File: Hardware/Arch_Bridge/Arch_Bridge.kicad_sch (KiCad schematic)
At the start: 91 parts, among them J1 Conn_01x02, J3 Conn_01x04, J4 Conn_01x04, Q1 2N3904, Q2 MJE2955, Q3 MJE2955, U1 AP63205WU, U11 ESP32-S3-WROOM-1, U12 TXS0102DCT, U13 DRV8231ADDAR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

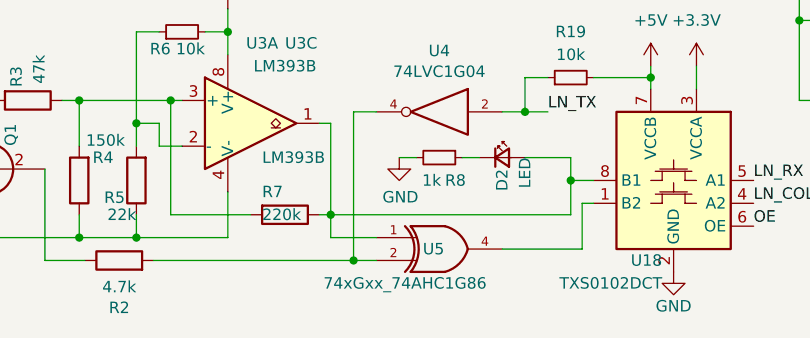
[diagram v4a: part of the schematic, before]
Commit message: More predictable Loconet TX_Q speeds. RX_Q similarly optimized, but continues to show high mS spike. Crashes on collision detect.
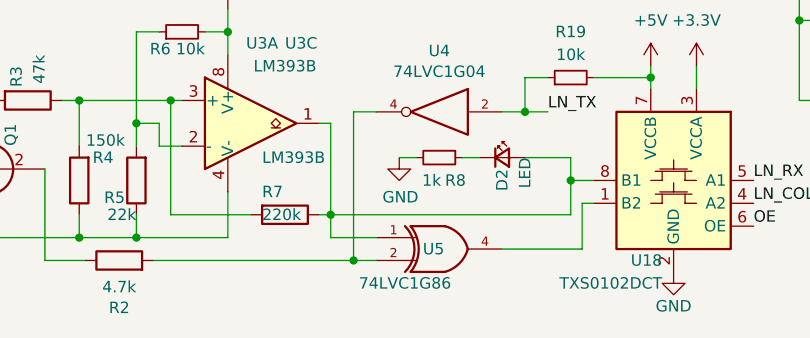
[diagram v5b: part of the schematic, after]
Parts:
- BOOT1, RESET1: LCSC SKU (none) -> C231329
- C1, C2, C3, C4: LCSC SKU (none) -> C2164091
- C10, C11, C5, C7, C8, C9, CU11, CU6: LCSC SKU (none) -> C600013
- C6: LCSC SKU (none) -> C2223641
- CB1: LCSC SKU (none) -> C2831718
- D3, D5: LCSC SKU (none) -> C895239
- D6: LCSC SKU (none) -> C523217
- D9: LCSC SKU (none) -> C552812
- F2, F3: LCSC SKU (none) -> C2442492
- F4: LCSC SKU (none) -> C2153889
- JP1: LCSC SKU (none) -> C5172712
- JP2, JP3: LCSC SKU (none) -> C3326988
- L1: LCSC SKU (none) -> C167828
- LOCONET_B1, LOCONET_B2, LOCONET_T1: LCSC SKU (none) -> C4355015
- Q1: LCSC SKU (none) -> C2980867
- Q2, Q3: LCSC SKU (none) -> C184196
- R1, R21, R24, R8: LCSC SKU (none) -> C131398
- R10: LCSC SKU (none) -> C488764
- R11, R12: LCSC SKU (none) -> C132648
- R13: LCSC SKU (none) -> C706423
- R14: LCSC SKU (none) -> C1391077
- R15: LCSC SKU (none) -> C872782
- R16, R17, R19, R20, R6: LCSC SKU (none) -> C4303232
- R18: LCSC SKU (none) -> C870936
- R2: LCSC SKU (none) -> C3975500
- R22, R23, R3: LCSC SKU (none) -> C137270
- R4: LCSC SKU (none) -> C114931
- R5: LCSC SKU (none) -> C114942
- R7: LCSC SKU (none) -> C130275
- R9: LCSC SKU (none) -> C601882; MFG YAEGO -> C601882
- U1: LCSC SKU (none) -> C2071056
- U11: LCSC SKU (none) -> C2980298
- U12, U17, U18: LCSC SKU (none) -> C2677354
- U19, U20: LCSC SKU (none) -> C17206
- U2: LCSC SKU (none) -> C91728
- U3: LCSC SKU (none) -> C2865059
- U4, U? (x2): LCSC SKU (none) -> C7827
- U5: value 74xGxx_74AHC1G86 -> 74LVC1G86; LCSC SKU (none) -> C402161; PN SN74LVC1G02DBVR -> SN74LVC1G86DBVR
- U6: LCSC SKU (none) -> C150160
- U? (x4): LCSC SKU (none) -> C2682152
- USB1: LCSC SKU (none) -> C136000

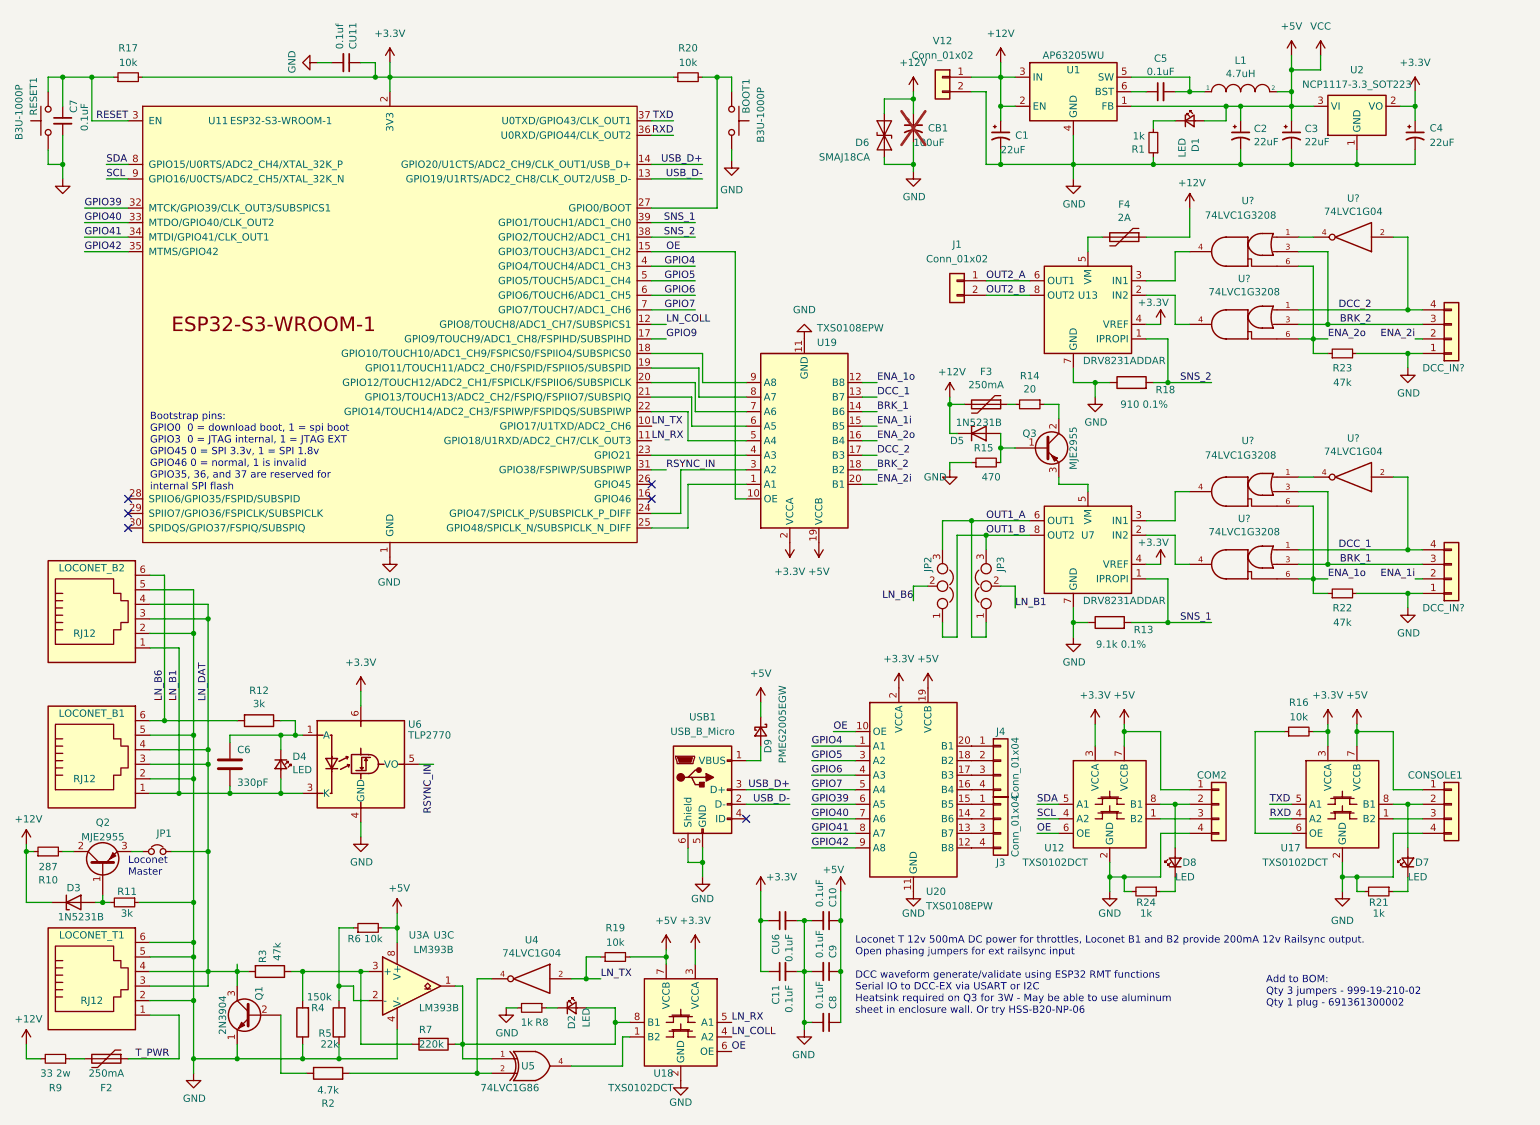
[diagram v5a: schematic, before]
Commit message: Schematic rev 0.8, PCB update adding current sense filter caps, fixing pull-up on Loconet TX, and slight reposition of U17
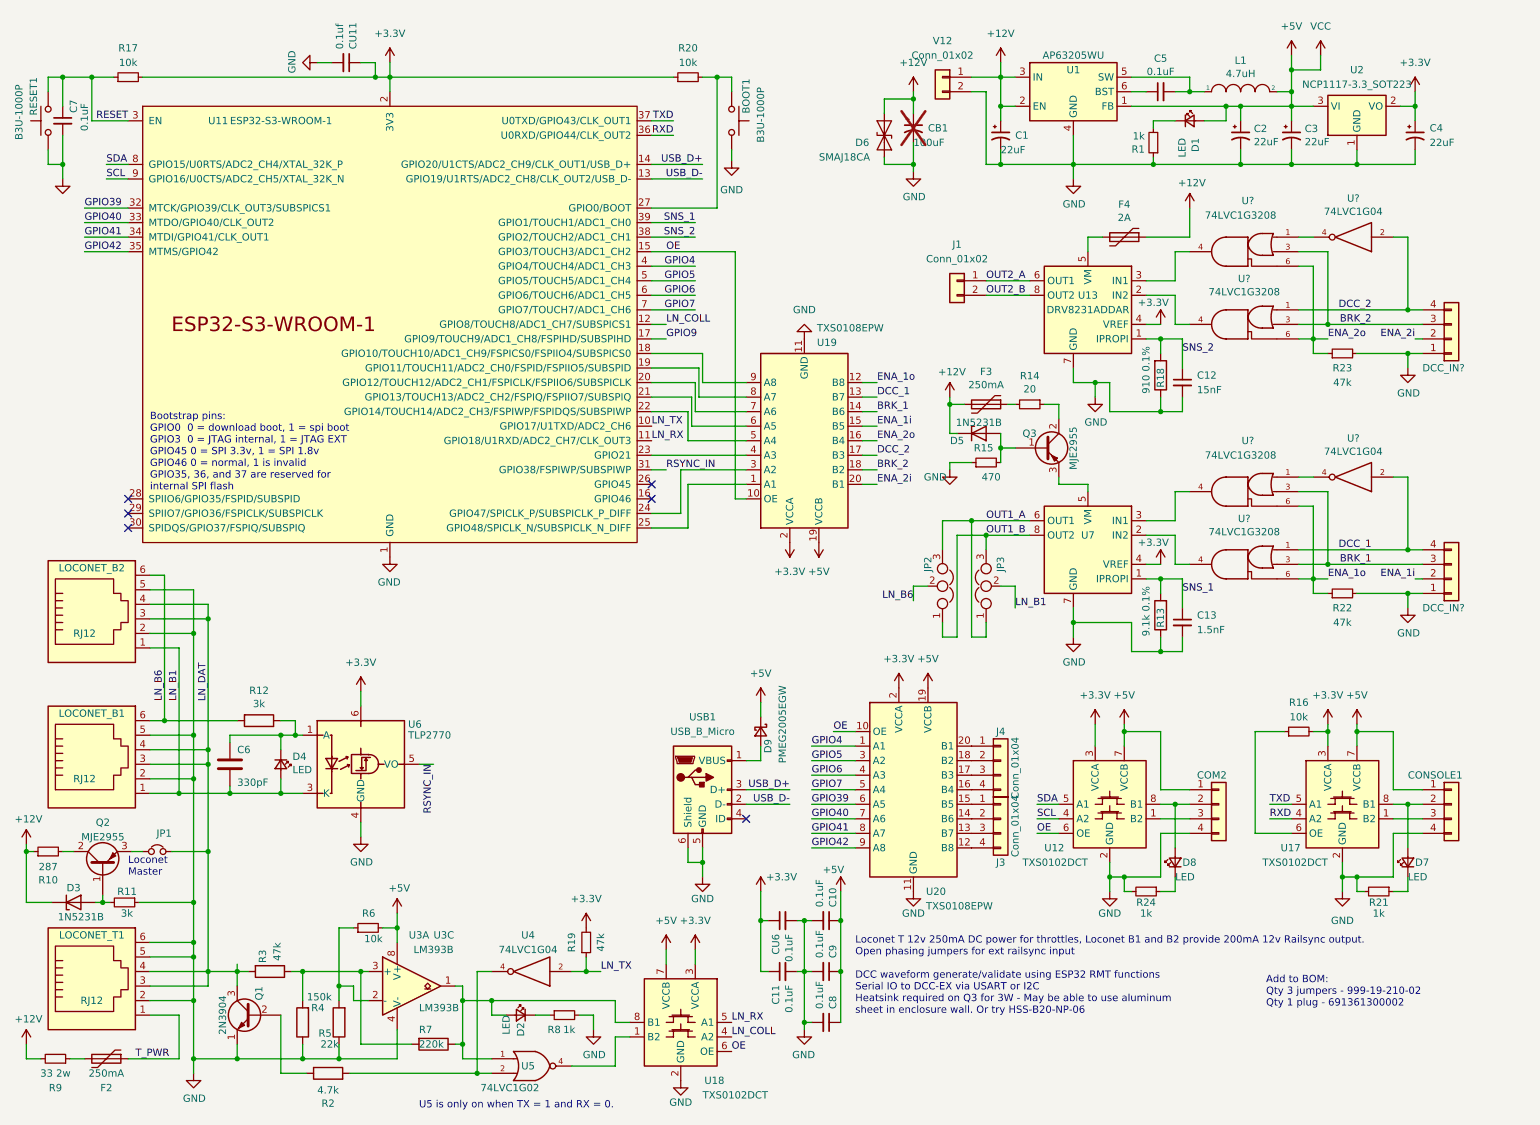
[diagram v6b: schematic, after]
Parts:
- added C12: 15nF, Capacitor_SMD:C_1206_3216Metric_Pad1.33x1.80mm_HandSolder, symbol Device:C_Small
- added C13: 1.5nF, Capacitor_SMD:C_1206_3216Metric_Pad1.33x1.80mm_HandSolder, symbol Device:C_Small
- R19: value 10k -> 47k; PN RC1206FR-1310KL -> RC1206FR-0747KL
- U5: value 74LVC1G86 -> 74LVC1G02; symbol Loconet DCC Interface-rescue:74AHC1G86-74xGxx -> Loconet DCC Interface-rescue:74AHCT1G02-74xGxx
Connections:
- net +3.3V: now also R19.2
- net +5V: no longer R19.2
- net GND: now also C12.2, C13.2
- net SNS_1: now also C13.1
- net SNS_2: now also C12.1
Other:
- note added: "Loconet T 12v 250mA DC power for throttles, Loconet B1 and B2 provide 200mA 12v Railsync output. Open phasing jumpers for ext railsync input DCC waveform generate/validate using ESP32 RMT functions Serial IO to DCC-EX via USART or I2C Heatsink required on Q3 for 3W - May be able to use aluminum sheet in enclosure wall. Or try HSS-B20-NP-06"
- note added: "U5 is only on when TX = 1 and RX = 0."
- note removed: "Loconet T 12v 500mA DC power for throttles, Loconet B1 and B2 provide 200mA 12v Railsync output. Open phasing jumpers for ext railsync input DCC waveform generate/validate using ESP32 RMT functions Serial IO to DCC-EX via USART or I2C Heatsink required on Q3 for 3W - May be able to use aluminum sheet in enclosure wall. Or try HSS-B20-NP-06"
- moved on the sheet: D2, R13, R18, R19, R8, U4

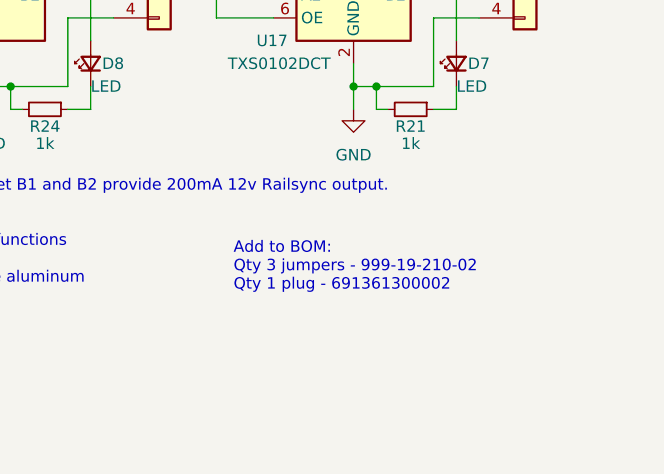
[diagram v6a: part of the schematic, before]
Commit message: Changed aux track output to use 5.0mm pitch matching EX-8874 track plugs
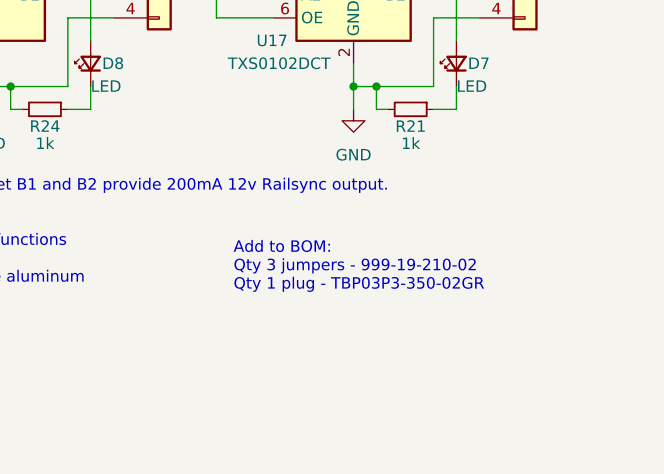
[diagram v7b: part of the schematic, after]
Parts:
- J1: footprint Terminal_Wuerth_new:WR-TBL 2P -> Connector_Phoenix_MC:PhoenixContact_MC_1,5_2-G-3.5_1x02_P3.50mm_Horizontal; LCSC SKU (none) -> C880572; MFG Wuerth Electronik -> CUI Inc; PN 691322310002 -> TBP03R1-350-02GR
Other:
- note added: "Add to BOM: Qty 3 jumpers - 999-19-210-02 Qty 1 plug - TBP03P3-350-02GR"
- note removed: "Add to BOM: Qty 3 jumpers - 999-19-210-02 Qty 1 plug - 691361300002"
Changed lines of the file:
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@@
     (effects (font (size 1.27 1.27)) (justify left bottom))
   )
-  (text "Add to BOM: \nQty 3 jumpers - 999-19-210-02\nQty 1 plug - 691361300002"
+  (text "Add to BOM: \nQty 3 jumpers - 999-19-210-02\nQty 1 plug - TBP03P3-350-02GR "
     (at 231.775 185.42 0)
     (effects (font (size 1.27 1.27)) (justify left bottom))
@@
       (effects (font (size 1.27 1.27)))
     )
-    (property "Footprint" "Terminal_Wuerth_new:WR-TBL 2P" (at 177.8 58.42 0)
+    (property "Footprint" "Connector_Phoenix_MC:PhoenixContact_MC_1,5_2-G-3.5_1x02_P3.50mm_Horizontal" (at 177.8 58.42 0)
       (effects (font (size 1.27 1.27)) hide)
     )
@@
       (effects (font (size 1.27 1.27)) hide)
     )
-    (property "MFG" "Wuerth Electronik" (at 177.8 58.42 0)
+    (property "MFG" "CUI Inc" (at 177.8 58.42 0)
       (effects (font (size 1.27 1.27)) hide)
     )
-    (property "PN" "691322310002 " (at 177.8 58.42 0)
+    (property "PN" "TBP03R1-350-02GR " (at 177.8 58.42 0)
       (effects (font (size 1.27 1.27)) hide)
     )
-    (property "LCSC SKU" "" (at 177.8 58.42 0)
+    (property "LCSC SKU" "C880572" (at 177.8 58.42 0)
       (effects (font (size 1.27 1.27)) hide)
     )

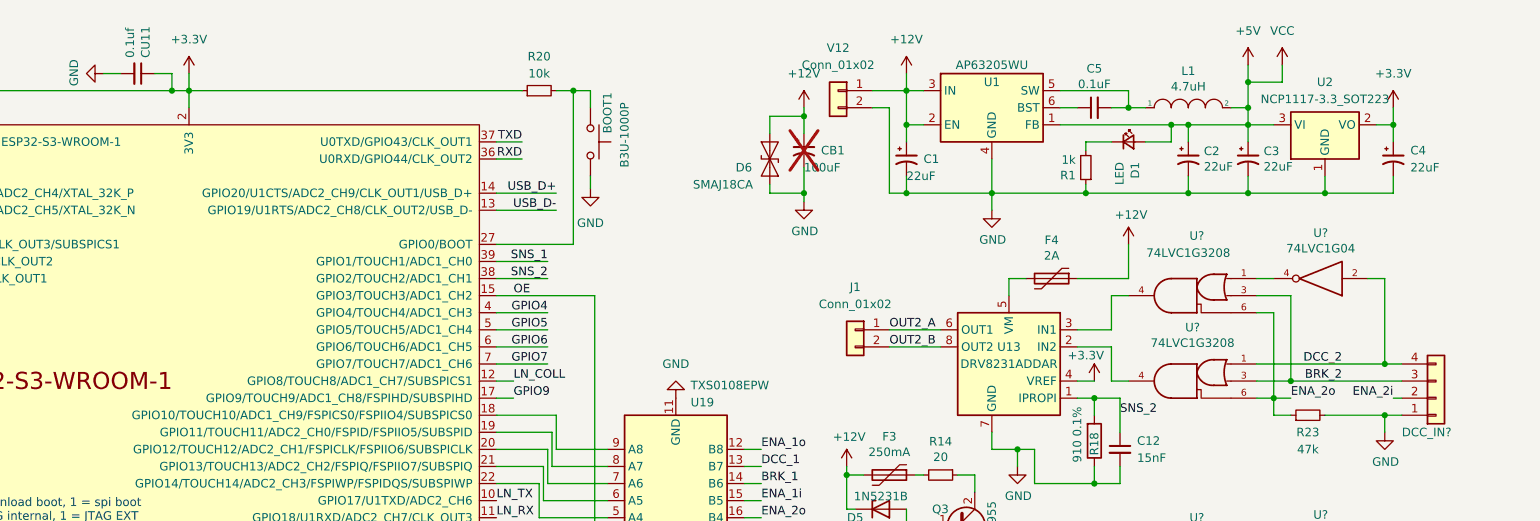
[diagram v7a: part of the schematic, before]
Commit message: Revised VIN to 5v power supply for better performance and less PCB space
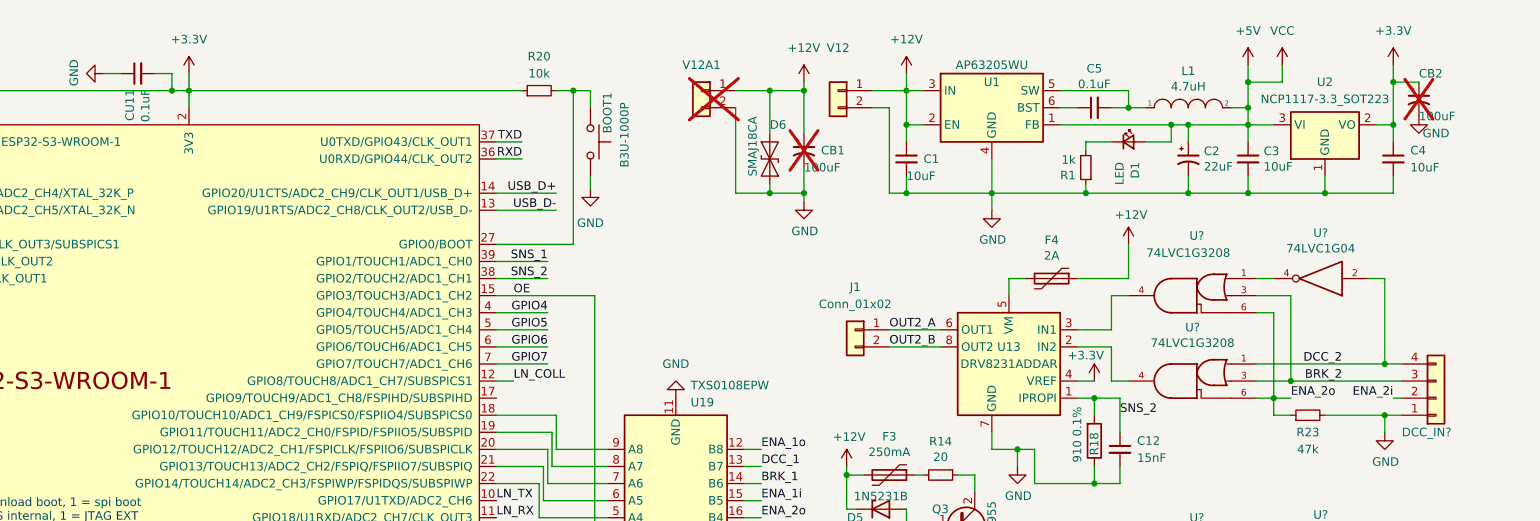
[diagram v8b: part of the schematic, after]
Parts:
- added CB2: 100uF, Capacitor_THT:CP_Radial_D6.3mm_P2.50mm, symbol Device:C_Polarized_Small_US
- added V12A1: Conn_01x02, Connector_Phoenix_MSTB:PhoenixContact_MSTBA_2,5_2-G_1x02_P5.00mm_Horizontal, symbol Connector_Generic:Conn_01x02
- C1, C3, C4: value 22uF -> 10uF; footprint Capacitor_SMD:CP_Elec_5x5.3 -> Capacitor_SMD:C_1210_3225Metric; symbol Device:C_Polarized_Small_US -> Device:C_Small; LCSC SKU C2164091 -> C2175202; MFG Wurth Electronik -> Murata; PN 865080542006 -> GRT31CR6YA106ME01L
- CU11: value 0.1uf -> 0.1uF
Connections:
- net +12V: now also V12A1.1 (Pin_1)
- net +3.3V: now also CU11.2, CB2.1; no longer CU11.1
- net GND: now also CU11.1, CB2.2, V12A1.2 (Pin_2); no longer CU11.2
- net GPIO9: no longer names the net of U11.17 (GPIO9/TOUCH9/ADC1_CH8/FSPIHD/SUBSPIHD)
